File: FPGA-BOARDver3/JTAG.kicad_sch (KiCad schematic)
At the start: 26 parts, among them J6 Conn_01x06_Pin, U1 XC7Z020-1CLG400I__, U4 ATSHA204A-SSHCZ-T, U7 S25FL128SAGMFI000

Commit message: update
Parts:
- D2: footprint LED_SMD:LED_0402_1005Metric -> footprints:LED_0402_1005Metric
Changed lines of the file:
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@@
 		(on_board yes)
 		(dnp no)
-		(fields_autoplaced yes)
 		(property "Reference" "U7"
-			(at 229.87 88.9 0)
+			(at 230.632 93.218 0)
 			(effects
 				(font
@@
 		)
 		(property "Value" "S25FL128SAGMFI000"
-			(at 229.87 91.44 0)
+			(at 230.886 96.266 0)
 			(effects
 				(font
@@
 			)
 		)
-		(property "Footprint" "LED_SMD:LED_0402_1005Metric"
+		(property "Footprint" "footprints:LED_0402_1005Metric"
 			(at 177.8 116.84 90)
 			(effects

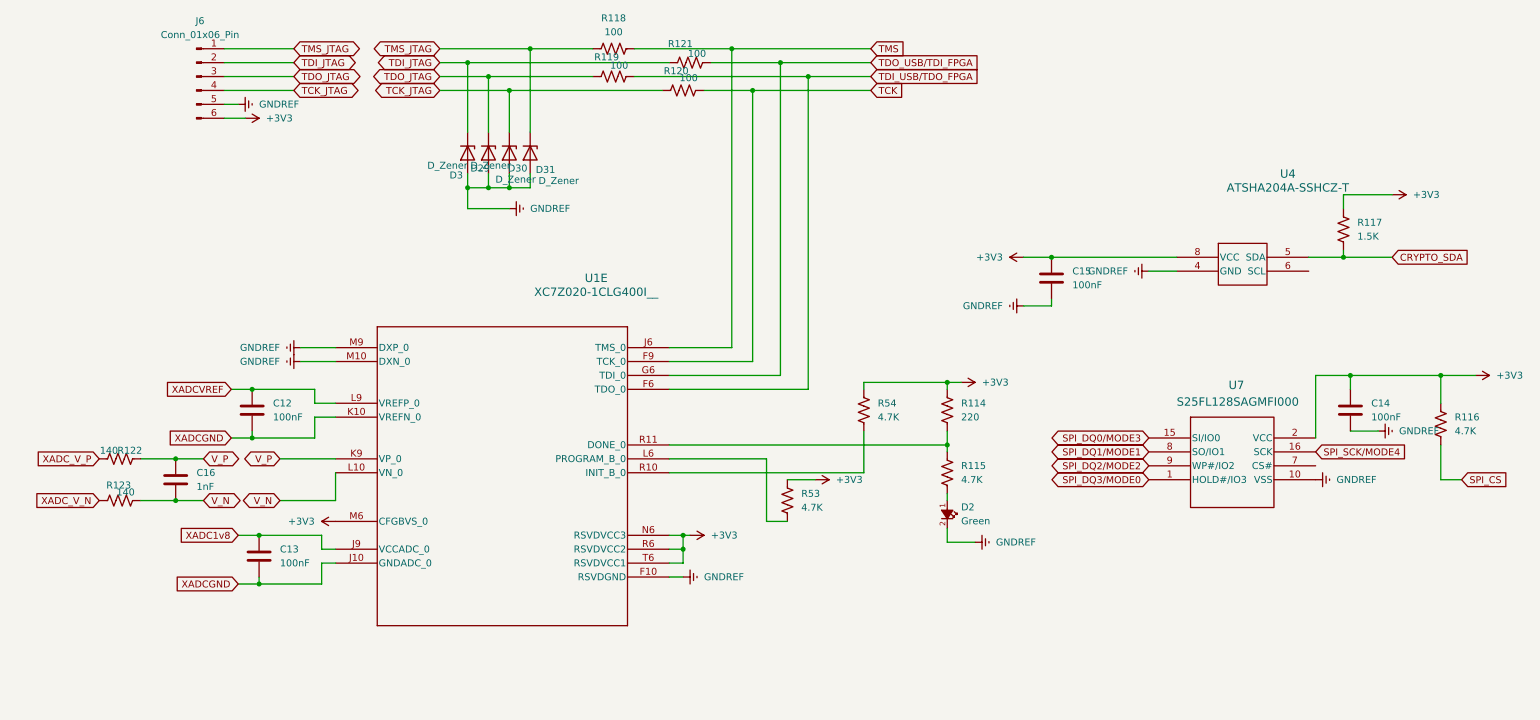
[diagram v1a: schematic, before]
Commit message: added audio out and usb
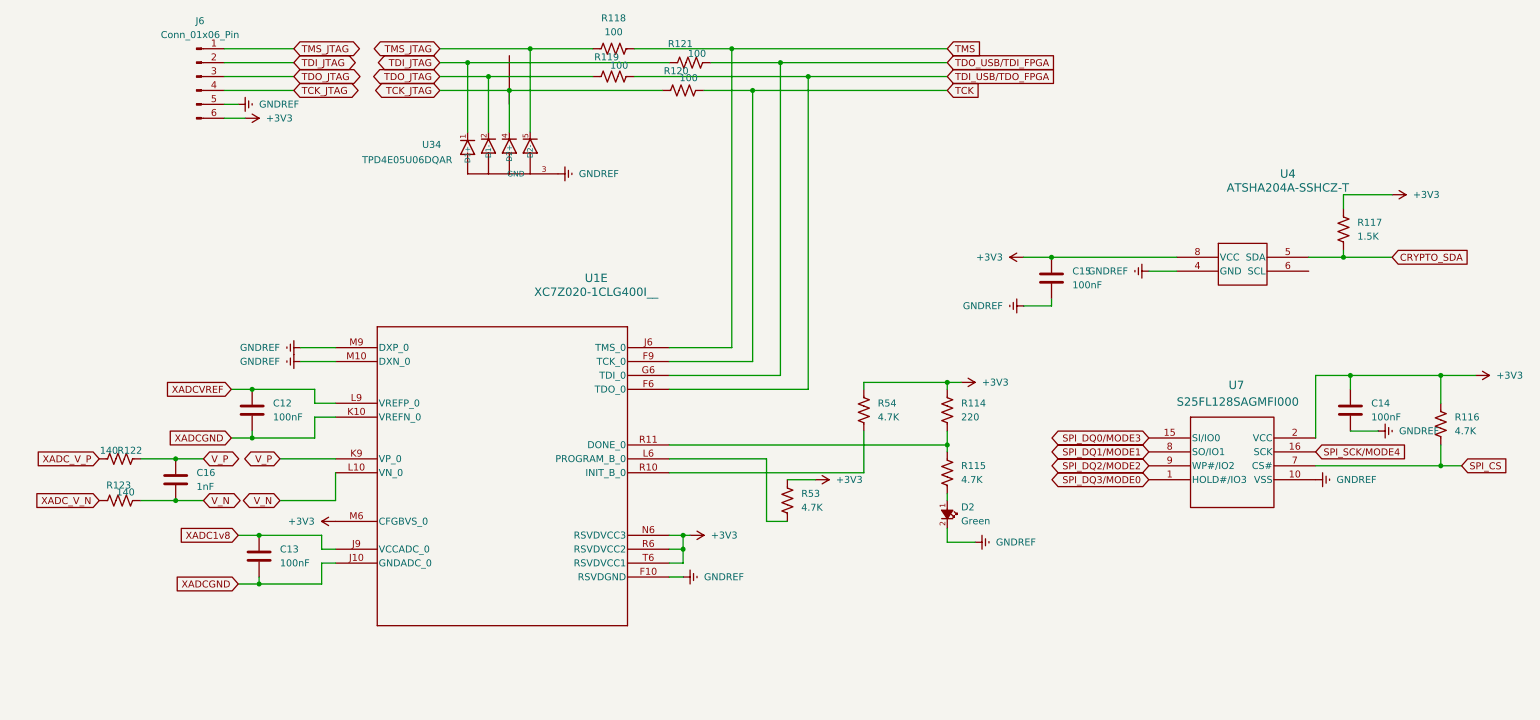
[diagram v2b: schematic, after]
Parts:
- removed D29, D3, D30, D31: D_Zener, footprints:SOD123_DIO, symbol Device:D_Zener
- added U34: TPD4E05U06DQAR, footprints:IC_TPD4E05U06DQAR, symbol TPD4E05U06DQAR:TPD4E05U06DQAR
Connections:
- net GNDREF: now also U34.3 (GND)
- net SPI_CS: now also U7.7 (CS#)
- net TCK_JTAG: now also U34.4 (D2+)
- net TDI_JTAG: now also U34.1 (D1+)
- net TDO_JTAG: now also U34.2 (D1-)
- net TMS_JTAG: now also U34.5 (D2-)
- new net GND__1: U34.8 (GND__1)

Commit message: updated schematic and layout
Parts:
- removed J6: Conn_01x06_Pin, footprints:CONN6_PZ254V-11-06P_XFC, symbol Connector:Conn_01x06_Pin
- removed U34: TPD4E05U06DQAR, footprints:IC_TPD4E05U06DQAR, symbol TPD4E05U06DQAR:TPD4E05U06DQAR
- C12, C13, C14, C15: LCSC PN (none) -> c1525
- C16: LCSC PN (none) -> c14442
- DONE1: renamed from D2; LCSC PN (none) -> C434449
- R114: LCSC PN (none) -> C112291
- R115: value 4.7K -> 220; LCSC PN (none) -> C112291
- R116, R53, R54: LCSC PN (none) -> C105871
- R117: LCSC PN (none) -> C114759
- R118, R119, R120, R121: LCSC PN (none) -> C106232
- R122, R123: LCSC PN (none) -> C327016
- U1: LCSC PN (none) -> C1519081
- U4: LCSC PN (none) -> C616025
- U7: LCSC PN (none) -> C393875
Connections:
- net TCK: no longer U1.F9 (TCK_0)
- net TMS: no longer U1.J6 (TMS_0)
- net TCK_JTAG: no longer names the net of R120.1
- net TCK_JTAG: now also U1.F9 (TCK_0)
- net TDI_JTAG: no longer names the net of R121.1
- net TDI_JTAG: now also U1.F6 (TDO_0)
- net TDI_USB/TDO_FPGA renamed TDI
- net TDI: no longer U1.F6 (TDO_0)
- net TDO_JTAG: no longer names the net of R119.1
- net TDO_JTAG: now also U1.G6 (TDI_0)
- net TDO_USB/TDI_FPGA renamed TDO
- net TDO: no longer U1.G6 (TDI_0)
- net TMS_JTAG: no longer names the net of R118.1
- net TMS_JTAG: now also U1.J6 (TMS_0)
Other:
- moved on the sheet: C12, C13, C16, DONE1, R114, R115, R118, R119, R120, R121, R122, R123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
